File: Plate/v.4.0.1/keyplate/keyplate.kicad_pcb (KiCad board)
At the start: 2 copper layers, 285.4 x 94.9 mm, 24 parts

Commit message: 廃止にともない、基板とプレートを接続するネジ穴を削除
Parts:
- removed the REF** at (54.3, 38.5)
- removed the REF** at (54.3, 57.5)
- removed the REF** at (59.1, 76.6)
- removed the REF** at (82.9, 76.6)
- removed the REF** at (101.0, 86.1)
- removed the REF** at (124.2, 86.1)
- removed the REF** at (230.5, 38.5)
- removed the REF** at (182.9, 76.6)
- removed the REF** at (221.0, 76.6)
- removed the REF** at (263.9, 76.6)
- removed the REF** at (273.4, 57.5)
- removed the REF** at (273.4, 38.5)
- removed the REF** at (273.4, 19.4)
- removed the REF** at (316.3, 19.4)
- removed the REF** at (147.2, 76.6)
- removed the REF** at (43.4, 50.9)
- removed the REF** at (135.3, 38.5)
- removed the REF** at (54.3, 19.4)
- removed the REF** at (43.4, 28.9)
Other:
- board text added: "#Jones_kbd Keyplate v.4.0.1 @jpskenn"
- board text removed: "#Jones_kbd Keyplate v.4.0.0 @jpskenn"

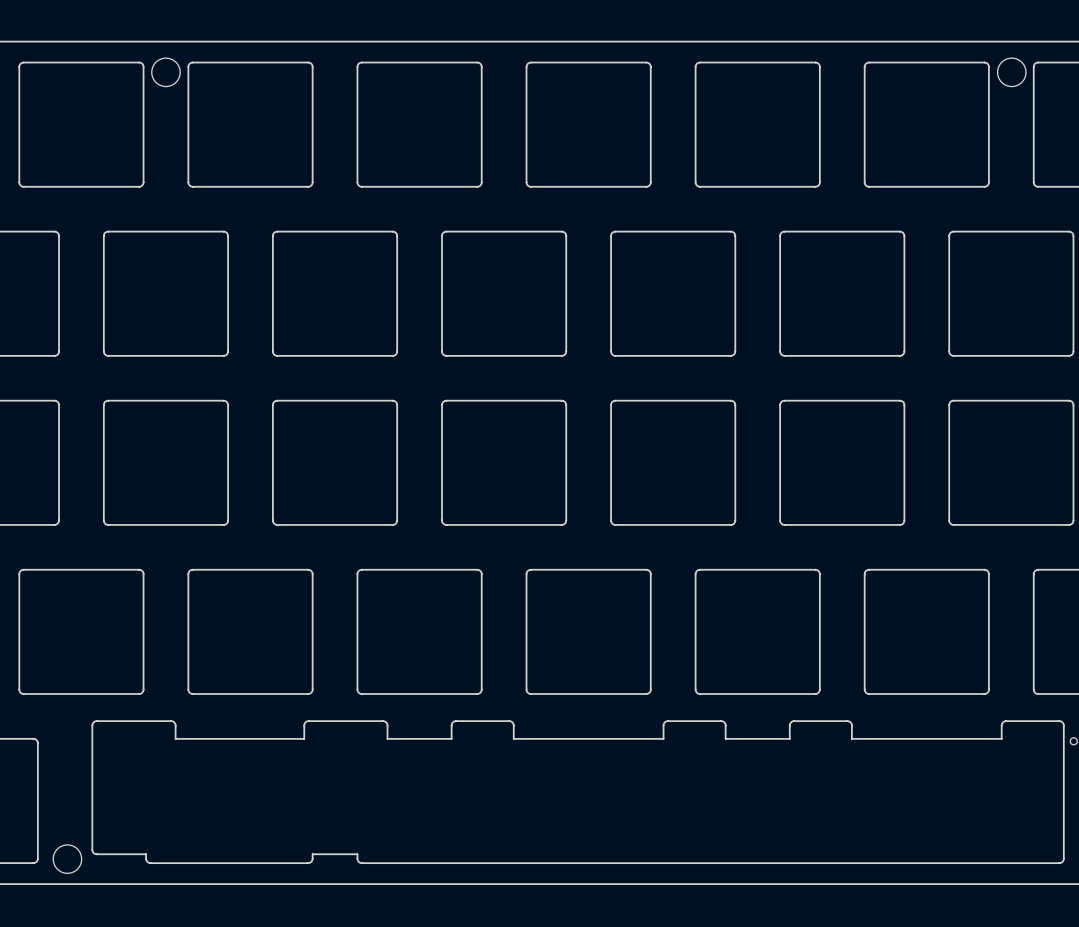
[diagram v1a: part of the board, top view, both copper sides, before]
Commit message: プレートのネジ穴位置調整など
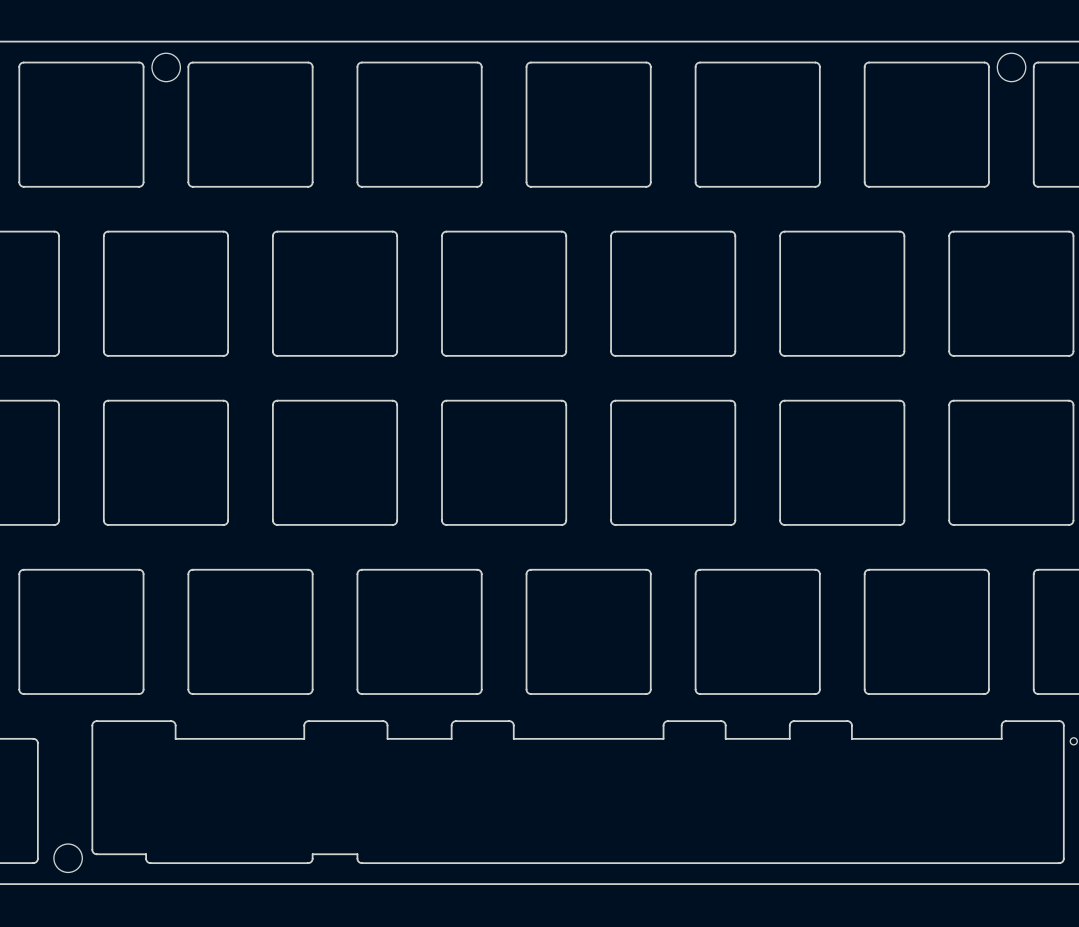
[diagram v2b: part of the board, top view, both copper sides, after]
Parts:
- added G***: LOGO, locallib:Jones_logo_7.8x13.2, B.Cu at (44.7, 23.8)
- moved REF** 0.55 mm to (230.6, 3.25)
- moved REF** 0.55 mm to (135.4, 3.25)
- moved REF** 0.13 mm to (124.3, 92.3)
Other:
- board text added: "#Jones_kbd Keyplate v.4.0.1, @jpskenn"
- board text added: "CUT HERE for NARROW LAYOUT"
- board text removed: "#Jones_kbd Keyplate v.4.0.1 @jpskenn"

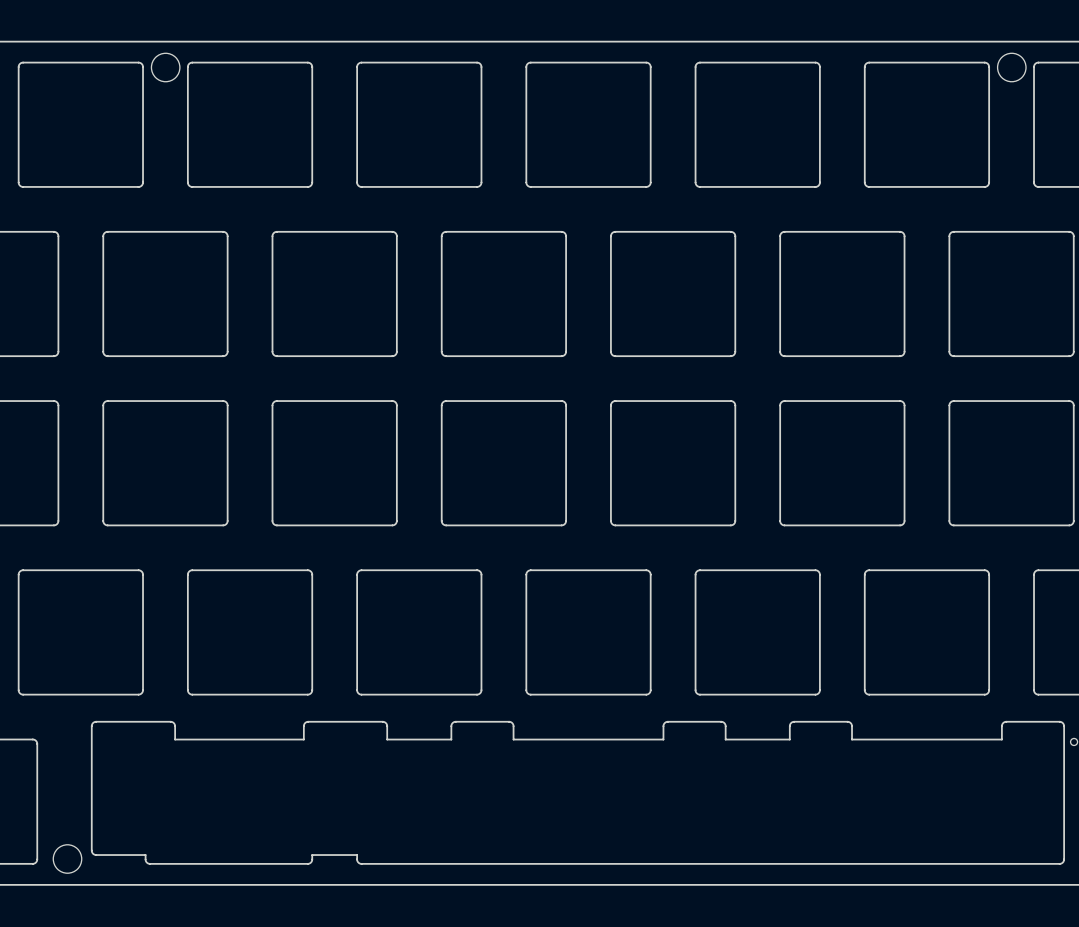
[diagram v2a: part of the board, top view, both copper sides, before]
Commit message: 基板とボトムをつなぐネジ位置の変更を反映
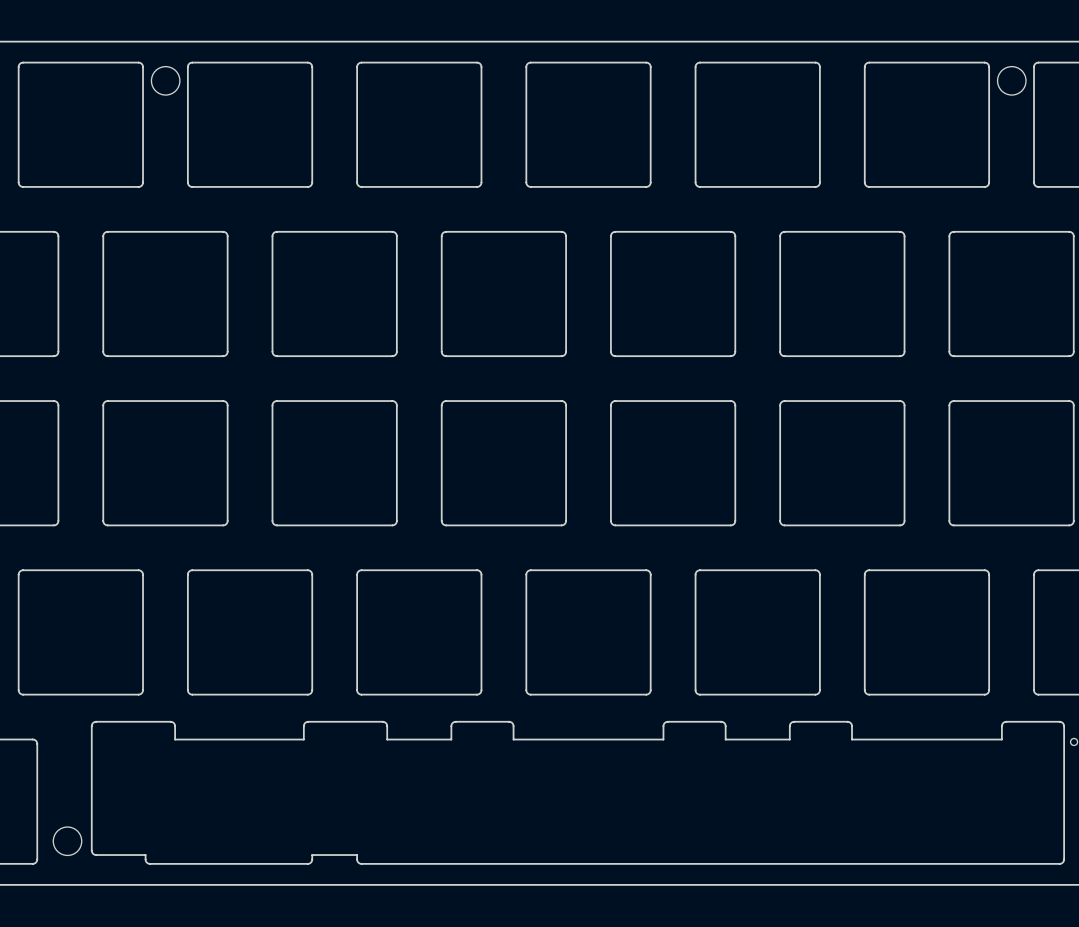
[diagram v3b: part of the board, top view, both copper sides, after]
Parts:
- moved REF** 2.00 mm to (124.3, 90.3)
- moved REF** 1.50 mm to (230.6, 4.75)
- moved REF** 1.50 mm to (135.4, 4.75)
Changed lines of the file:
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@@
   )
   (module MountingHole:MountingHole_3.2mm_M3 (layer F.Cu)
-    (at 124.325 92.34948)
+    (at 124.325 90.34948)
+    (descr "Mounting Hole 3.2mm, no annular, M3")
+    (tags "mounting hole 3.2mm no annular m3")
+    (attr virtual)
+    (fp_text reference REF** (at 0 -4.2) (layer F.SilkS) hide
+      (effects (font (size 1 1) (thickness 0.15)))
+    )
+    (fp_text value MountingHole_3.2mm_M3 (at 0 4.2) (layer F.Fab)
+      (effects (font (size 1 1) (thickness 0.15)))
+    )
+    (fp_circle (center 0 0) (end 3.2 0) (layer Cmts.User) (width 0.15))
+    (fp_circle (center 0 0) (end 3.45 0) (layer F.CrtYd) (width 0.05))
+    (fp_text user %R (at 0.3 0) (layer F.Fab)
+      (effects (font (size 1 1) (thickness 0.15)))
+    )
+    (pad 1 np_thru_hole circle (at 0 0) (size 3.2 3.2) (drill 3.2) (layers *.Cu *.Mask))
+  )
+  (module MountingHole:MountingHole_3.2mm_M3 (layer F.Cu)
+    (at 230.625 4.74948)
     (descr "Mounting Hole 3.2mm, no annular, M3")
     (tags "mounting hole 3.2mm no annular m3")
@@
   )
   (module MountingHole:MountingHole_3.2mm_M3 (layer F.Cu)
-    (at 230.625 3.24948)
-    (descr "Mounting Hole 3.2mm, no annular, M3")
-    (tags "mounting hole 3.2mm no annular m3")
-    (attr virtual)
-    (fp_text reference REF** (at 0 -4.2) (layer F.SilkS) hide
-      (effects (font (size 1 1) (thickness 0.15)))
-    )
-    (fp_text value MountingHole_3.2mm_M3 (at 0 4.2) (layer F.Fab)
-      (effects (font (size 1 1) (thickness 0.15)))
-    )
-    (fp_circle (center 0 0) (end 3.2 0) (layer Cmts.User) (width 0.15))
-    (fp_circle (center 0 0) (end 3.45 0) (layer F.CrtYd) (width 0.05))
-    (fp_text user %R (at 0.3 0) (layer F.Fab)
-      (effects (font (size 1 1) (thickness 0.15)))
-    )
-    (pad 1 np_thru_hole circle (at 0 0) (size 3.2 3.2) (drill 3.2) (layers *.Cu *.Mask))
-  )
-  (module MountingHole:MountingHole_3.2mm_M3 (layer F.Cu)
-    (at 135.375 3.24948)
+    (at 135.375 4.74948)
     (descr "Mounting Hole 3.2mm, no annular, M3")
     (tags "mounting hole 3.2mm no annular m3")
@@
   (gr_arc (start 237.5 80.5) (end 237.5 80.3) (angle -90) (layer B.SilkS) (width 0.12))
   (gr_arc (start 244 80.5) (end 244.2 80.5) (angle -90) (layer B.SilkS) (width 0.12))
-  (gr_text "CUT HERE\nfor\nNARROW\nLAYOUT" (at 240.8 80.6 90) (layer B.SilkS)
-    (effects (font (size 1 1) (thickness 0.15)) (justify left mirror))
+  (gr_text "CUT HERE\nfor\nNARROW\nLAYOUT" (at 240.8 84.8 90) (layer B.SilkS)
+    (effects (font (size 1 1) (thickness 0.15)) (justify mirror))
   )
   (gr_line (start 244 80.3) (end 237.5 80.3) (layer B.SilkS) (width 0.12))

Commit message: レイアウト変更をプレートに反映
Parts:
- removed the REF** at (124.3, 90.3)
- removed the REF** at (230.6, 4.75)
- removed the REF** at (135.4, 4.75)
- removed the REF** at (240.2, 78.9)
- added REF**: MountingHole_3.2mm_M3, MountingHole:MountingHole_3.2mm_M3, F.Cu at (110.2, 19.9)
- added REF**: MountingHole_3.2mm_M3, MountingHole:MountingHole_3.2mm_M3, F.Cu at (99.2, 105.5)
- added REF**: MountingHole_3.2mm_M3, MountingHole:MountingHole_3.2mm_M3, F.Cu at (205.5, 19.9)
- moved G*** 29.3 mm to (19.6, 38.9)
- moved REF** 29.3 mm to (40.5, 43.5)
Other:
- outline, holes or cut-outs redrawn
- board text removed: "CUT HERE for NARROW LAYOUT"

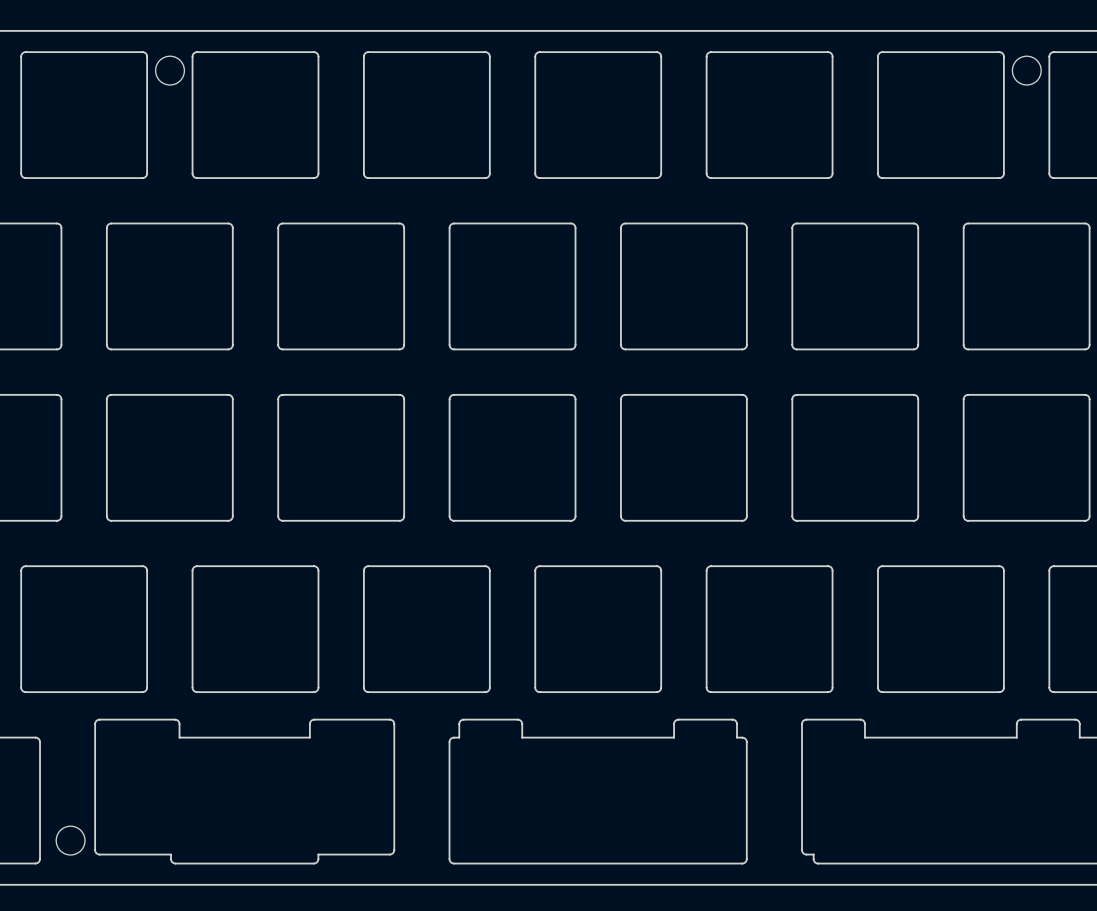
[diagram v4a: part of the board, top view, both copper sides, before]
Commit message: ボトムプレートへのネジ穴アクセス用の穴を拡大
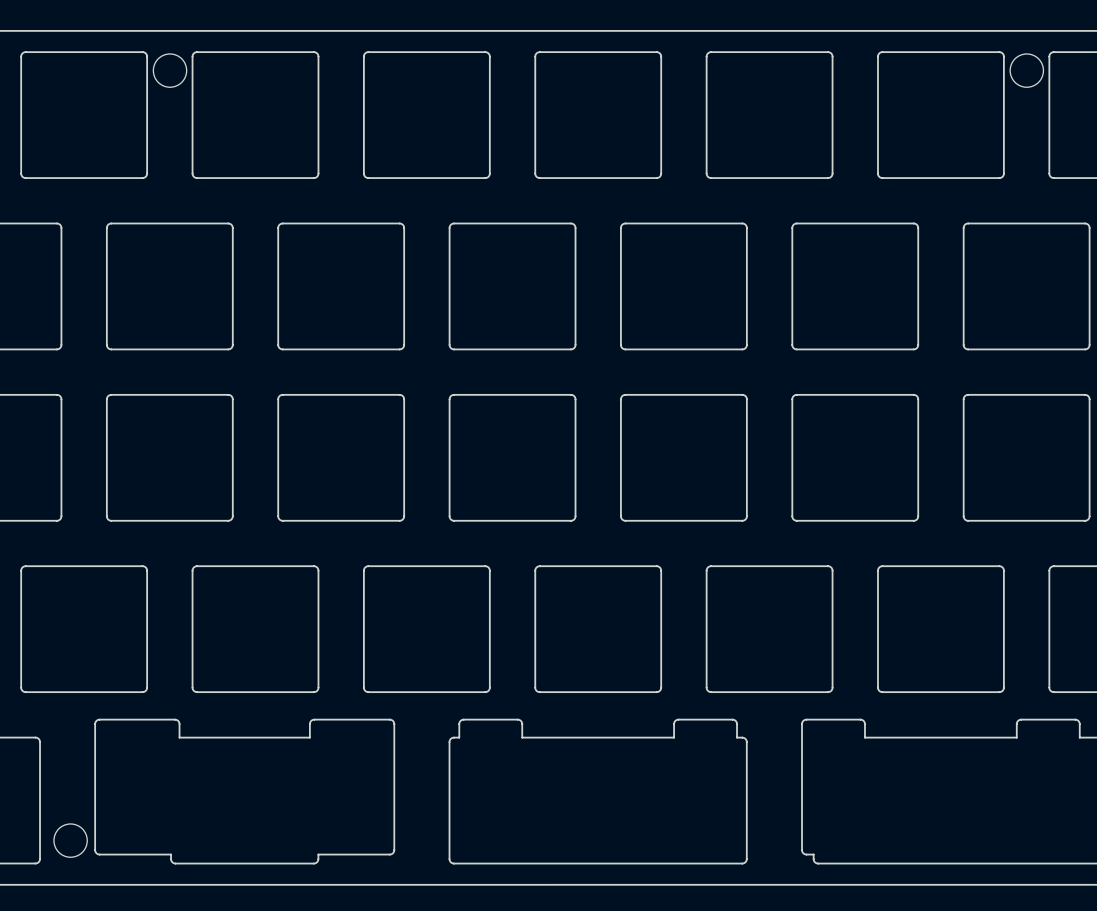
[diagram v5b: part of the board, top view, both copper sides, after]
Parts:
- removed the G*** at (19.6, 38.9)
- added G***: LOGO, locallib:Jones_logo_B_8.3x13.9, B.Cu at (19.7, 39.1)
- REF** (x3): value MountingHole_3.2mm_M3 -> MountingHole_3.7mm; footprint MountingHole:MountingHole_3.2mm_M3 -> MountingHole:MountingHole_3.7mm
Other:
- board text added: "#Jones_kbd Keyplate v.4.0.2, @jpskenn"
- board text removed: "#Jones_kbd Keyplate v.4.0.1, @jpskenn"

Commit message: ボトムプレートへのネジ穴アクセスを、枠の一部をカットして実現。
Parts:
- removed the REF** at (110.2, 19.9)
- removed the REF** at (99.2, 105.5)
- removed the REF** at (205.5, 19.9)
- moved G*** 2.80 mm to (22.5, 38.8)
- moved REF** 2.78 mm to (43.3, 43.2)
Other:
- outline, holes or cut-outs redrawn
